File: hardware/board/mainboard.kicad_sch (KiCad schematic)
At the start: 0 parts

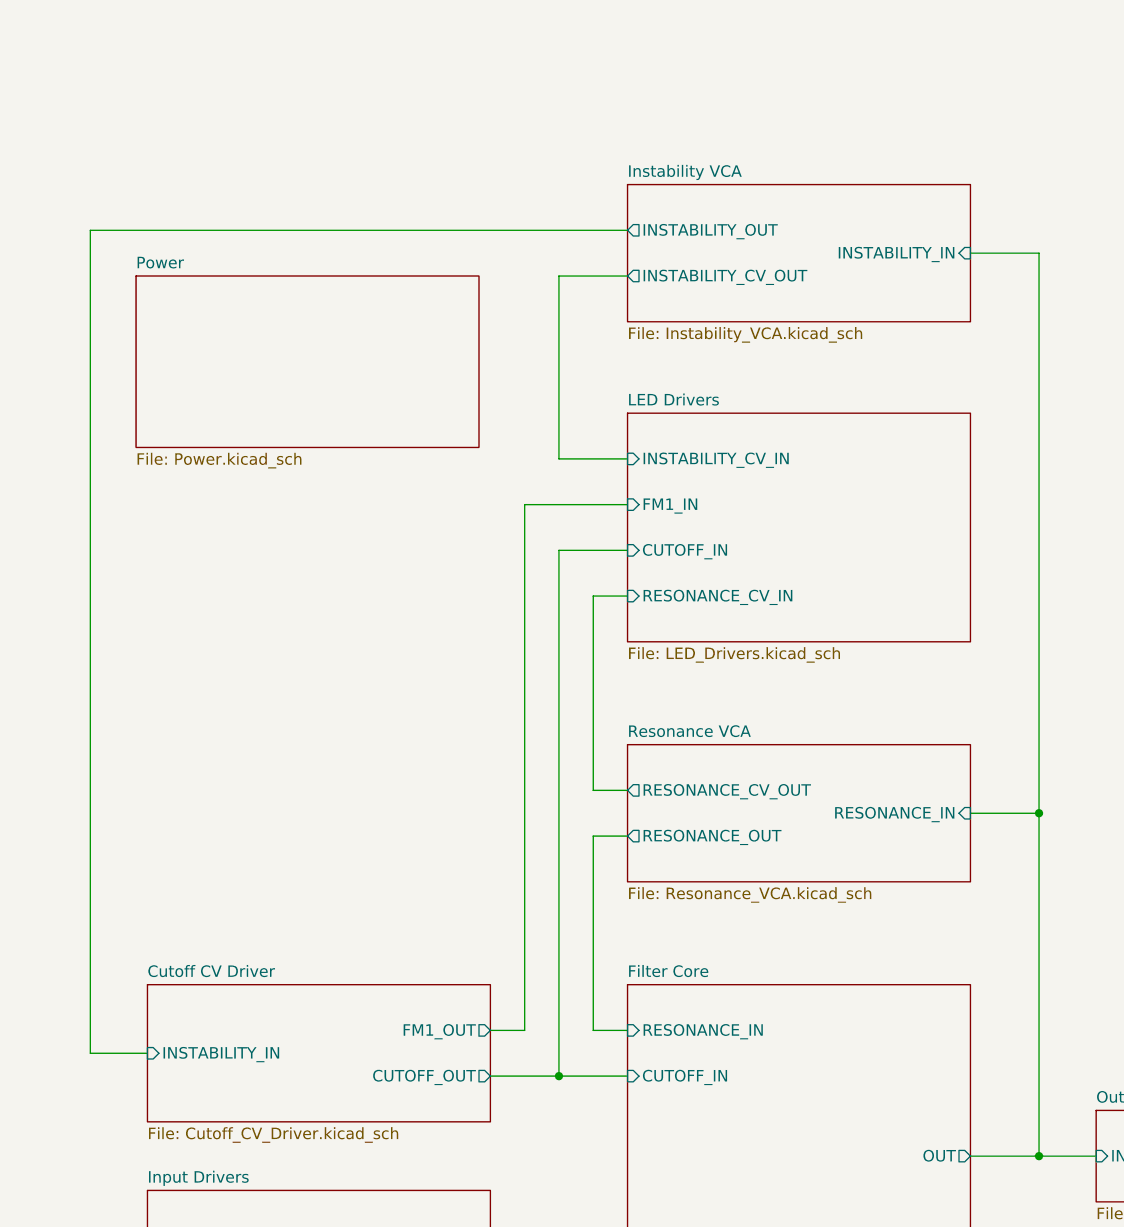
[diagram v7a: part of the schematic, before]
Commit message: Updated PCB to add and routed new components.
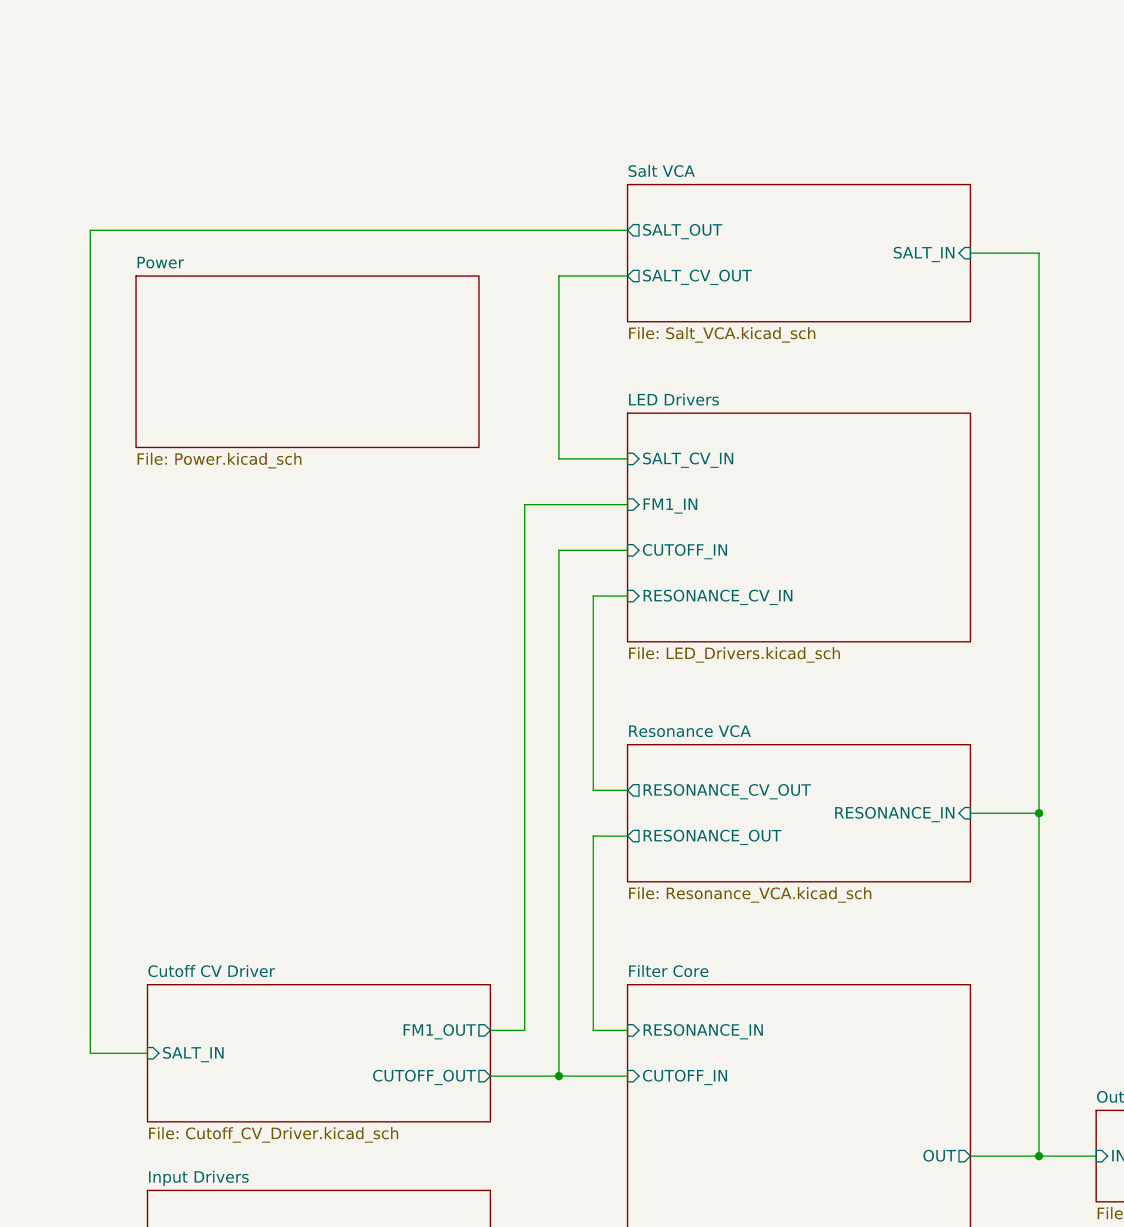
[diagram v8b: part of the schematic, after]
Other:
- sheet Instability VCA renamed Salt VCA
- sheet Cutoff CV Driver ports: added SALT_IN; removed INSTABILITY_IN
- sheet LED Drivers ports: added SALT_CV_IN; removed INSTABILITY_CV_IN
- sheet Salt VCA: file Instability_VCA.kicad_sch -> Salt_VCA.kicad_sch
- sheet Salt VCA ports: added SALT_CV_OUT, SALT_IN, SALT_OUT; removed INSTABILITY_CV_OUT, INSTABILITY_IN, INSTABILITY_OUT
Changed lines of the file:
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@@
   (title_block
     (title "Neptune")
-    (date "2023-07-20")
+    (date "2023-09-26")
     (rev "v0")
     (company "Winterbloom")
@@
     (stroke (width 0.1524) (type solid))
     (fill (color 0 0 0 0.0000))
-    (property "Sheetname" "Instability VCA" (at 130.81 34.8484 0)
-      (effects (font (size 1.27 1.27)) (justify left bottom))
-    )
-    (property "Sheetfile" "Instability_VCA.kicad_sch" (at 130.81 51.3846 0)
-      (effects (font (size 1.27 1.27)) (justify left top))
-    )
-    (pin "INSTABILITY_OUT" output (at 130.81 40.64 180)
-      (effects (font (size 1.27 1.27)) (justify left))
-    )
-    (pin "INSTABILITY_IN" input (at 168.91 43.18 0)
-      (effects (font (size 1.27 1.27)) (justify right))
-    )
-    (pin "INSTABILITY_CV_OUT" output (at 130.81 45.72 180)
+    (property "Sheetname" "Salt VCA" (at 130.81 34.8484 0)
+      (effects (font (size 1.27 1.27)) (justify left bottom))
+    )
+    (property "Sheetfile" "Salt_VCA.kicad_sch" (at 130.81 51.3846 0)
+      (effects (font (size 1.27 1.27)) (justify left top))
+    )
+    (pin "SALT_OUT" output (at 130.81 40.64 180)
+      (effects (font (size 1.27 1.27)) (justify left))
+    )
+    (pin "SALT_IN" input (at 168.91 43.18 0)
+      (effects (font (size 1.27 1.27)) (justify right))
+    )
+    (pin "SALT_CV_OUT" output (at 130.81 45.72 180)
       (effects (font (size 1.27 1.27)) (justify left))
     )
@@
       (effects (font (size 1.27 1.27)) (justify right))
     )
-    (pin "INSTABILITY_IN" input (at 77.47 132.08 180)
-      (effects (font (size 1.27 1.27)) (justify left))
-    )
     (pin "FM1_OUT" output (at 115.57 129.54 0)
       (effects (font (size 1.27 1.27)) (justify right))
     )
+    (pin "SALT_IN" input (at 77.47 132.08 180)
+      (effects (font (size 1.27 1.27)) (justify left))
+    )
     (instances
       (project "mainboard"
@@
       (effects (font (size 1.27 1.27)) (justify left))
     )
-    (pin "INSTABILITY_CV_IN" input (at 130.81 66.04 180)
-      (effects (font (size 1.27 1.27)) (justify left))
-    )
     (pin "FM1_IN" input (at 130.81 71.12 180)
       (effects (font (size 1.27 1.27)) (justify left))
     )
+    (pin "SALT_CV_IN" input (at 130.81 66.04 180)
+      (effects (font (size 1.27 1.27)) (justify left))
+    )
